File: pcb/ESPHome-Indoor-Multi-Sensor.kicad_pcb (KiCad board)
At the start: 4 copper layers, 52.5 x 59.7 mm, 110 parts, among them J1 SEN66, J2 USB-C, J3 SEN0609, J4 LD2410, J5 SPKR, J6 LD2450, Q1 MMBFJ201, SW1 BOOT, SW2 RESET, T1 Tab, T10 Tab, T2 Tab, T3 Tab, T4 Tab, T5 Tab, T6 Tab, T7 Tab, T8 Tab, T9 Tab, U1 SN74LV1T34DBV, U10 SCD41, U11 BMP581, U12 MCP6042, U13 ADS1115, U14 SHT45, U15 EKMC1603111, U16 TGS5141, U17 DS18S20, U2 TLV62568DRL, U3 MAX98357A, U4 TLV75533PDRV, U5 TLV62568DRL, U6 ESP32-S3-WROOM-2-N32R16V, U7 INA228, U8 TSL2591, U9 SGP41

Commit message: Add new ina228 to other power supplies
Not finished
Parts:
- removed JP1: Gain, TMM-105-01-X-D-SM:SAMTEC_TMM-105-01-X-D-SM
- added C40: 100nF, Capacitor_SMD:C_0402_1005Metric, F.Cu at (116.9, 60.3)
- added C41: 100nF, Capacitor_SMD:C_0402_1005Metric, F.Cu at (114.6, 50.4)
- added U18: INA228, Package_SO:VSSOP-10_3x3mm_P0.5mm, F.Cu at (116.8, 57.9)
- added U19: INA228, Package_SO:VSSOP-10_3x3mm_P0.5mm, F.Cu at (114.6, 52.7)
- R10, R8: value 10Ω -> 150mΩ; footprint Resistor_SMD:R_0402_1005Metric -> Resistor_SMD:R_0603_1608Metric
- R9: footprint Resistor_SMD:R_1210_3225Metric -> Resistor_SMD:R_0805_2012Metric
- moved R11 12.1 mm to (117.1, 49.1)
- moved R8 10.5 mm to (111.7, 58.7), turned to 180 degrees
- moved R10 9.59 mm to (109.4, 53.6), turned to 180 degrees
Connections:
- C14 pad 2: +3.3VA -> Net-(U19-Vbus)
- C15 pad 1: +3.3VA -> Net-(U19-Vbus)
- C17 pad 2: +3.3V -> Net-(U18-Vbus)
- C18 pad 1: +3.3V -> Net-(U18-Vbus)
- C19 pad 1: +3.3V -> Net-(U18-Vbus)
- L2 pad 2: +3.3V -> Net-(U18-Vbus)
- R10 pad 1: /VBUS -> Net-(U19-Vbus)
- R10 pad 2: Net-(U7-Vin+) -> +3.3VA
- R11 pad 1: Net-(JP1-Pin_10) -> GND
- R4 pad 1: +3.3V -> Net-(U18-Vbus)
- R8 pad 1: +5V -> Net-(U18-Vbus)
- R8 pad 2: Net-(U7-Vin-) -> +3.3V
- U4 pad 1: +3.3VA -> Net-(U19-Vbus)
- U7 pad 10: Net-(U7-Vin+) -> /VBUS
- U7 pad 9: Net-(U7-Vin-) -> +5V
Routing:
- net Net-(U3-GAIN_SLOT): track 19.7 -> 1.25 mm, vias 2 -> 1
- net +5V: track 46.3 -> 28.5 mm, vias 32 -> 31
- net Net-(JP1-Pin_10): track 15.8 -> 0.00 mm
- net +3.3V: track 17.5 -> 7.65 mm, vias 19 -> 17
- net Net-(U18-Vbus): track 0.00 -> 9.89 mm, vias 0 -> 2
- net /VBUS: track 13.4 -> 7.98 mm
- net Net-(U7-Vin-): track 3.67 -> 0.00 mm
- net Net-(U7-Vin+): track 3.17 -> 0.00 mm
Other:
- board text removed: "12dB"
- board text removed: "15dB"
- board text removed: "3dB"
- board text removed: "6dB"
- board text removed: "9dB"
- board text removed: "SPKR Gain"

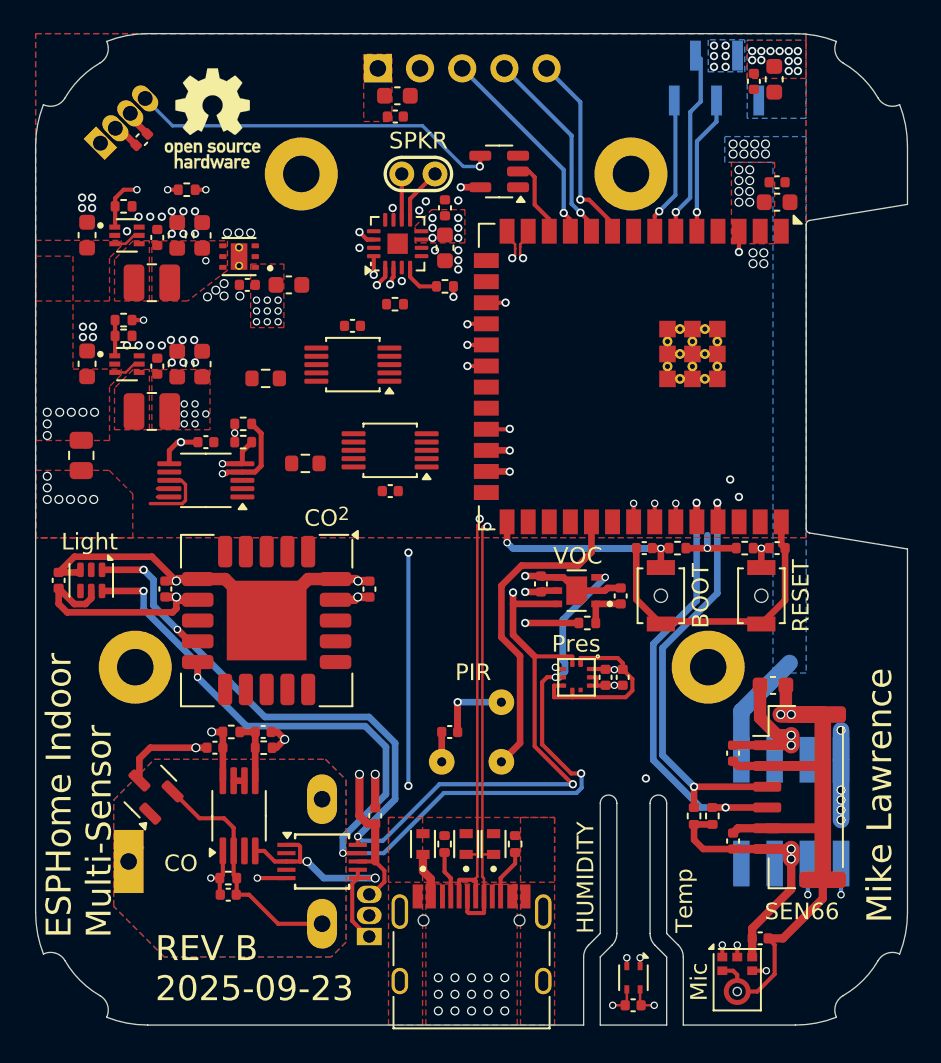
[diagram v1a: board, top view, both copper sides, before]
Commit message: Rev B Updates finish adding power monitors for 3.3V and 3.3VA
Removed speaker gain jumper
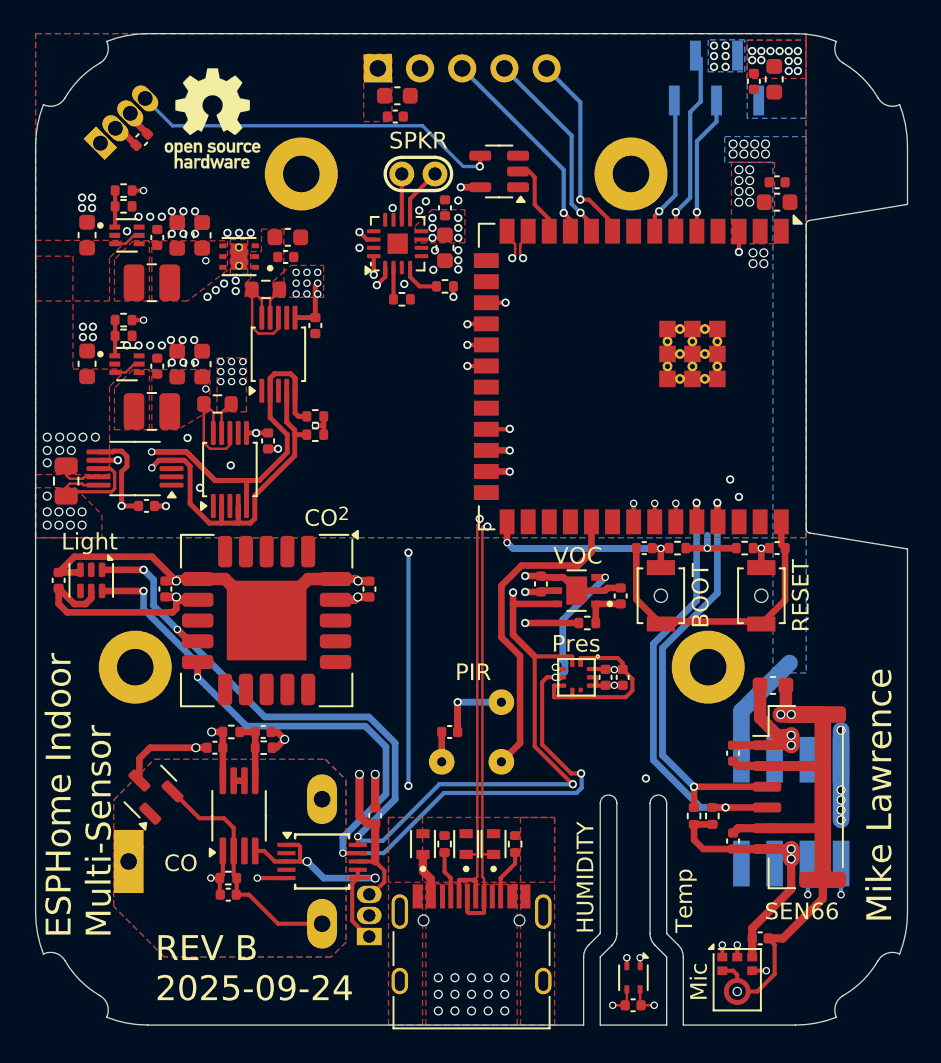
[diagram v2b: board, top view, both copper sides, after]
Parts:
- R10: value 150mΩ -> 80mΩ
- R8: value 150mΩ -> 68mΩ
- moved U18 9.72 mm to (107.2, 59.0), turned to 90 degrees
- moved C40 7.95 mm to (109.5, 57.3), turned to 90 degrees
- moved R8 6.39 mm to (106.5, 55.1), turned to 0 degrees
- moved R10 5.36 mm to (109.4, 48.2), turned to 0 degrees
- moved C20 5.24 mm to (102.2, 61.2)
- moved R7 4.61 mm to (112.3, 55.9), turned to 180 degrees
- moved U19 4.53 mm to (110.1, 52.1), turned to 90 degrees
- moved R6 4.39 mm to (112.3, 56.9), turned to 180 degrees
- moved U7 4.32 mm to (101.5, 59.0)
- moved R1 3.80 mm to (100.8, 42.2)
- moved C15 2.87 mm to (110.7, 45.1)
- moved C14 2.86 mm to (110.6, 46.2), turned to 180 degrees
- moved C41 2.24 mm to (112.3, 50.4), turned to 90 degrees
- moved R9 1.79 mm to (97.3, 59.7)
- moved R11 0.51 mm to (117.6, 48.8)
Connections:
- net +3.6V renamed /Power Supplies/+3.6V_SRC
- net Net-(U18-Vbus) renamed /Power Supplies/+3.3V_SRC
- net Net-(U19-Vbus) renamed /Power Supplies/+3.3VA_SRC
- C40 pad 2: +3.3V -> +3.3VA
- C41 pad 2: +3.3V -> +3.3VA
- U18 pad 2: Net-(U18-A0) -> /SDA1
- U18 pad 4: Net-(U18-A0) -> /SDA1
- U18 pad 5: unconnected-(U18-SCL-Pad5) -> /SCL1
- U18 pad 6: +3.3V -> +3.3VA
- U19 pad 2: Net-(U19-A0) -> /SCL1
- U19 pad 4: unconnected-(U19-SDA-Pad4) -> /SDA1
- U19 pad 5: Net-(U19-A0) -> /SCL1
- U19 pad 6: +3.3V -> +3.3VA
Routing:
- net /SCL1: track 101.5 -> 123.6 mm
- net /SDA1: track 105.7 -> 120.8 mm
- net +3.3VA: track 115.7 -> 125.4 mm, vias 22 -> 23
- net /Power Supplies/+3.3VA_SRC: track 0.00 -> 6.74 mm
- net +3.3V: track 7.65 -> 13.5 mm, vias 17 -> 20
- net /Power Supplies/+3.3V_SRC: track 9.89 -> 15.3 mm
- net +5V: track 28.5 -> 24.4 mm, vias 31 -> 33
- net Net-(U2-FB): track 5.75 -> 2.20 mm, vias 2 -> 0
- net /Power Supplies/+3.6V_SRC: track 4.92 -> 8.45 mm
- net /VBUS: track 7.98 -> 10.5 mm, vias 22 -> 24
- net GND: track 162.7 -> 165.2 mm, vias 78 -> 85
- net I2S1_WS: track 15.4 -> 14.5 mm
- net Net-(U3-GAIN_SLOT): track 1.25 -> 1.91 mm, vias 1 -> 0
- added copper zone on F.Cu, net /Power Supplies/+3.3VA_SRC
- added copper zone on F.Cu, net /Power Supplies/+3.3V_SRC
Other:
- board text added: "REV B 2025-09-24"
- board text removed: "REV B 2025-09-23"

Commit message: Design now uses one ina228 and two ina232 power sensors
Reduces cost without sacrificing functionality. Mainly wanted power supply voltage and currents.
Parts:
- U18, U19: value INA228 -> INA238
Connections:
- net /1Wire renamed /1WIRE
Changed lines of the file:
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@@
 	(net 77 "/ESP32-S3/SEN0609_EN")
 	(net 78 "/ESP32-S3/LD24X0_EN")
-	(net 79 "/1Wire")
+	(net 79 "/1WIRE")
 	(net 80 "/Power Supplies/+3.3VA_SRC")
 	(net 81 "/Power Supplies/+3.3V_SRC")
@@
 			)
 		)
-		(property "Value" "INA228"
+		(property "Value" "INA238"
 			(at 0 2.450001 90)
 			(layer "F.Fab")
@@
 			)
 		)
-		(property "Description" "IC, High-Side or Low-Side Measurement, Bi-Directional Current and Power Monitor (0-85V) with I2C, SMBus-, and PMBus-Compatible Interface, VSSOP-10"
+		(property "Description" "IC, 85V, 16-Bit, High-Precision Power Monitor With I2C Interface, VSSOP-10"
 			(at 0 0 90)
 			(layer "F.Fab")
@@
 			)
 		)
-		(property "Part Number" "INA228AIDGSR"
+		(property "Part Number" "INA238AIDGSR"
 			(at 0 0 90)
 			(unlocked yes)
@@
 			)
 		)
-		(property "Description" "IC, High-Side or Low-Side Measurement, Bi-Directional Current and Power Monitor (0-85V) with I2C, SMBus-, and PMBus-Compatible Interface, VSSOP-10"
+		(property "Description" "IC, 85-V, 20-Bit, Ultra-Precise Power-Energy-Charge Monitor With I2C Interface, VSSOP-10"
 			(at 0 0 0)
 			(layer "F.Fab")
@@
 			)
 		)
-		(property "Value" "INA228"
+		(property "Value" "INA238"
 			(at 0 2.450001 90)
 			(layer "F.Fab")
@@
 			)
 		)
-		(property "Description" "IC, High-Side or Low-Side Measurement, Bi-Directional Current and Power Monitor (0-85V) with I2C, SMBus-, and PMBus-Compatible Interface, VSSOP-10"
+		(property "Description" "IC, 85V, 16-Bit, High-Precision Power Monitor With I2C Interface, VSSOP-10"
 			(at 0 0 90)
 			(layer "F.Fab")
@@
 			)
 		)
-		(property "Part Number" "INA228AIDGSR"
+		(property "Part Number" "INA238AIDGSR"
 			(at 0 0 90)
 			(unlocked yes)
@@
 			(size 1.5 0.9)
 			(layers "F.Cu" "F.Mask" "F.Paste")
-			(net 79 "/1Wire")
+			(net 79 "/1WIRE")
 			(pinfunction "IO21")
 			(pintype "bidirectional")
@@
 			(layers "*.Cu" "*.Mask")
 			(remove_unused_layers no)
-			(net 79 "/1Wire")
+			(net 79 "/1WIRE")
 			(pinfunction "DQ")
 			(pintype "bidirectional")
@@
 		(name "$teardrop_padvia$")
 		(hatch none 0.1)
-		(priority 30004)
-		(attr
-			(teardrop
-				(type padvia)
-			)
-		)
-		(connect_pads yes
-			(clearance 0)
-		)
-		(min_thickness 0.0254)
-		(filled_areas_thickness no)
-		(fill yes
-			(thermal_gap 0.5)
-			(thermal_bridge_width 0.5)
-			(island_removal_mode 1)
-			(island_area_min 10)
-		)
-		(polygon
-			(pts
-				(xy 121.875 83.94) (xy 121.881772 83.964271) (xy 121.890841 84.007842) (xy 121.880077 84.023745)
-				(xy 121.85 84.03) (xy 122 84.756) (xy 122.15 84.03) (xy 122.123105 84.025435) (xy 122.110813 84.013478)
-				(xy 122.112615 83.980396) (xy 122.118228 83.964271) (xy 122.125 83.94)
-			)
-		)
-	)
-	(zone
-		(net 27)
-		(net_name "/D-")
-		(layer "F.Cu")
-		(name "$teardrop_padvia$")
-		(hatch none 0.1)
 		(priority 30007)
 		(attr
@@
 	)
 	(zone
-		(net 26)
-		(net_name "/D+")
-		(layer "F.Cu")
-		(name "$teardrop_padvia$")
-		(hatch none 0.1)
-		(priority 30002)
-		(attr
-			(teardrop
-				(type padvia)
-			)
-		)
-		(connect_pads yes
-			(clearance 0)
-		)
-		(min_thickness 0.0254)
-		(filled_areas_thickness no)
-		(fill yes
-			(thermal_gap 0.5)
-			(thermal_bridge_width 0.5)
-			(island_removal_mode 1)
-			(island_area_min 10)
-		)
-		(polygon
-			(pts
-				(xy 121.625 85.57) (xy 121.618228 85.545729) (xy 121.609159 85.502158) (xy 121.619923 85.486255)
-				(xy 121.65 85.48) (xy 121.5 84.754) (xy 121.35 85.48) (xy 121.376895 85.484565) (xy 121.389187 85.496522)
-				(xy 121.387385 85.529604) (xy 121.381772 85.545729) (xy 121.375 85.57)
-			)
-		)
-	)
-	(zone
 		(net 2)
 		(net_name "+5V")
@@
 	)
 	(zone
-		(net 27)
-		(net_name "/D-")
+		(net 80)
+		(net_name "/Power Supplies/+3.3VA_SRC")
 		(layer "F.Cu")
-		(name "$teardrop_padvia$")
-		(hatch none 0.1)
-		(priority 30005)
-		(attr
-			(teardrop
-				(type padvia)
-			)
-		)
+		(name "Top Ground")
+		(hatch edge 0.5)
+		(priority 3)
 		(connect_pads yes
 			(clearance 0)
 		)
-		(min_thickness 0.0254)
+		(min_thickness 0.15)
 		(filled_areas_thickness no)
 		(fill yes
 			(thermal_gap 0.5)
 			(thermal_bridge_width 0.5)
-			(island_removal_mode 1)
-			(island_area_min 10)
 		)
 		(polygon
 			(pts
-				(xy 120.875 83.94) (xy 120.881772 83.964271) (xy 120.890841 84.007842) (xy 120.880077 84.023745)
-				(xy 120.85 84.03) (xy 121 84.756) (xy 121.15 84.03) (xy 121.123105 84.025435) (xy 121.110813 84.013478)
-				(xy 121.112615 83.980396) (xy 121.118228 83.964271) (xy 121.125 83.94)
+				(xy 108.125 47.825) (xy 108.45 47.55) (xy 108.45 45.925) (xy 109.1 45.925) (xy 109.1 44.575) (xy 110.45 44.575)
+				(xy 110.45 48.675) (xy 108.125 48.675)
 			)
 		)
 	)
 	(zone
-		(net 80)
-		(net_name "/Power Supplies/+3.3VA_SRC")
+		(net 8)
+		(net_name "/Power Supplies/SW_3V6")
 		(layer "F.Cu")
 		(name "Top Ground")
 		(hatch edge 0.5)
-		(priority 3)
+		(priority 2)
 		(connect_pads yes
 			(clearance 0)
@@
 		(polygon
 			(pts
-				(xy 108.125 47.825) (xy 108.45 47.55) (xy 108.45 45.925) (xy 109.1 45.925) (xy 109.1 44.575) (xy 110.45 44.575)
-				(xy 110.45 48.675) (xy 108.125 48.675)
+				(xy 101.375 45.275) (xy 100.25 46.4) (xy 100.25 48.9) (xy 102.35 48.9) (xy 102.35 45.275)
 			)
 		)
 	)
 	(zone
-		(net 11)
-		(net_name "Net-(J2-CC2)")
+		(net 27)
+		(net_name "/D-")
 		(layer "F.Cu")
 		(name "$teardrop_padvia$")
 		(hatch none 0.1)
-		(priority 30000)
+		(priority 30004)
 		(attr
 			(teardrop
@@
 		(polygon
 			(pts
-				(xy 123.375 83.94) (xy 123.381772 83.964271) (xy 123.390841 84.007842) (xy 123.380077 84.023745)
-				(xy 123.35 84.03) (xy 123.5 84.756) (xy 123.65 84.03) (xy 123.623105 84.025435) (xy 123.610813 84.013478)
-				(xy 123.612615 83.980396) (xy 123.618228 83.964271) (xy 123.625 83.94)
-			)
-		)
-	)
-	(zone
-		(net 8)
-		(net_name "/Power Supplies/SW_3V6")
-		(layer "F.Cu")
-		(name "Top Ground")
-		(hatch edge 0.5)
-		(priority 2)
-		(connect_pads yes
-			(clearance 0)
-		)
-		(min_thickness 0.15)
-		(filled_areas_thickness no)
-		(fill yes
-			(thermal_gap 0.5)
-			(thermal_bridge_width 0.5)
-		)
-		(polygon
-			(pts
-				(xy 101.375 45.275) (xy 100.25 46.4) (xy 100.25 48.9) (xy 102.35 48.9) (xy 102.35 45.275)
+				(xy 121.875 83.94) (xy 121.881772 83.964271) (xy 121.890841 84.007842) (xy 121.880077 84.023745)
+				(xy 121.85 84.03) (xy 122 84.756) (xy 122.15 84.03) (xy 122.123105 84.025435) (xy 122.110813 84.013478)
+				(xy 122.112615 83.980396) (xy 122.118228 83.964271) (xy 122.125 83.94)
 			)
 		)
@@
 	)
 	(zone
+		(net 27)
+		(net_name "/D-")
+		(layer "F.Cu")
+		(name "$teardrop_padvia$")
+		(hatch none 0.1)
+		(priority 30005)
+		(attr
+			(teardrop
+				(type padvia)
+			)
+		)
+		(connect_pads yes
+			(clearance 0)
+		)
+		(min_thickness 0.0254)
+		(filled_areas_thickness no)
+		(fill yes
+			(thermal_gap 0.5)
+			(thermal_bridge_width 0.5)
+			(island_removal_mode 1)
+			(island_area_min 10)
+		)
+		(polygon
+			(pts
+				(xy 120.875 83.94) (xy 120.881772 83.964271) (xy 120.890841 84.007842) (xy 120.880077 84.023745)
+				(xy 120.85 84.03) (xy 121 84.756) (xy 121.15 84.03) (xy 121.123105 84.025435) (xy 121.110813 84.013478)
+				(xy 121.112615 83.980396) (xy 121.118228 83.964271) (xy 121.125 83.94)
+			)
+		)
+	)
+	(zone
 		(net 1)
 		(net_name "GND")
@@
 		(name "$teardrop_padvia$")
 		(hatch none 0.1)
-		(priority 30006)
+		(priority 30002)
 		(attr
 			(teardrop
@@
 		(polygon
 			(pts
-				(xy 122.4238 83.94) (xy 122.423801 83.941354) (xy 122.414603 83.996772) (xy 122.392692 84.02031)
-				(xy 122.35 84.03) (xy 122.5 84.756) (xy 122.65 84.03) (xy 122.618684 84.02542) (xy 122.597778 84.013358)
-				(xy 122.578486 83.975317) (xy 122.576199 83.941354) (xy 122.5762 83.94)
+				(xy 121.625 85.57) (xy 121.618228 85.545729) (xy 121.609159 85.502158) (xy 121.619923 85.486255)
+				(xy 121.65 85.48) (xy 121.5 84.754) (xy 121.35 85.48) (xy 121.376895 85.484565) (xy 121.389187 85.496522)
+				(xy 121.387385 85.529604) (xy 121.381772 85.545729) (xy 121.375 85.57)
 			)
 		)
@@
 	)
 	(zone
+		(net 26)
+		(net_name "/D+")
+		(layer "F.Cu")
+		(name "$teardrop_padvia$")
+		(hatch none 0.1)
+		(priority 30006)
+		(attr
+			(teardrop
+				(type padvia)
+			)
+		)
+		(connect_pads yes
+			(clearance 0)
+		)
+		(min_thickness 0.0254)
+		(filled_areas_thickness no)
+		(fill yes
+			(thermal_gap 0.5)
+			(thermal_bridge_width 0.5)
+			(island_removal_mode 1)
+			(island_area_min 10)
+		)
+		(polygon
+			(pts
+				(xy 122.4238 83.94) (xy 122.423801 83.941354) (xy 122.414603 83.996772) (xy 122.392692 84.02031)
+				(xy 122.35 84.03) (xy 122.5 84.756) (xy 122.65 84.03) (xy 122.618684 84.02542) (xy 122.597778 84.013358)
+				(xy 122.578486 83.975317) (xy 122.576199 83.941354) (xy 122.5762 83.94)
+			)
+		)
+	)
+	(zone
 		(net 32)
 		(net_name "/VBUS")
@@
 			)
 		)
+	)
+	(zone
+		(net 11)
+		(net_name "Net-(J2-CC2)")
+		(layer "F.Cu")
+		(name "$teardrop_padvia$")
+		(hatch none 0.1)
+		(priority 30000)
+		(attr
+			(teardrop
+				(type padvia)
+			)
+		)
+		(connect_pads yes
+			(clearance 0)
+		)
+		(min_thickness 0.0254)
+		(filled_areas_thickness no)
+		(fill yes
+			(thermal_gap 0.5)
+			(thermal_bridge_width 0.5)
+			(island_removal_mode 1)
+			(island_area_min 10)
+		)
+		(polygon
+			(pts
+				(xy 123.375 83.94) (xy 123.381772 83.964271) (xy 123.390841 84.007842) (xy 123.380077 84.023745)
+				(xy 123.35 84.03) (xy 123.5 84.756) (xy 123.65 84.03) (xy 123.623105 84.025435) (xy 123.610813 84.013478)
+				(xy 123.612615 83.980396) (xy 123.618228 83.964271) (xy 123.625 83.94)
+			)
+		)
